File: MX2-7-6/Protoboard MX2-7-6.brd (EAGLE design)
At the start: 54.2 x 59.2 mm, 294 parts

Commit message: Update Gerb files
Created Gerber files for MX 2-7-6 without ESP
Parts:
- added U2: (no value), SparkFun-PowerIC:SOT23-5
- moved PAD442 1.27 mm to (27.9, 7.62)
- moved PAD443 1.27 mm to (40.6, 7.62)
- moved PAD444 1.27 mm to (5.08, 7.62)
- moved PAD445 1.27 mm to (43.2, 7.62)
- moved PAD446 1.27 mm to (38.1, 7.62)
- moved PAD447 1.27 mm to (7.62, 7.62)
- moved PAD448 1.27 mm to (50.8, 7.62)
- moved PAD449 1.27 mm to (35.6, 7.62)
- moved PAD450 1.27 mm to (10.2, 7.62)
- moved PAD451 1.27 mm to (48.3, 7.62)
- moved PAD452 1.27 mm to (33.0, 7.62)
- moved PAD453 1.27 mm to (12.7, 7.62)
- moved PAD454 1.27 mm to (45.7, 7.62)
- moved PAD455 1.27 mm to (30.5, 7.62)
- moved PAD456 1.27 mm to (15.2, 7.62)
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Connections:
- net GND: now also U2.2
- net VCC: now also U2.1, U2.3
- net VDD: now also U2.5
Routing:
- net VCC: track 12.5 -> 23.9 mm
- net VDD: track 133.6 -> 138.2 mm

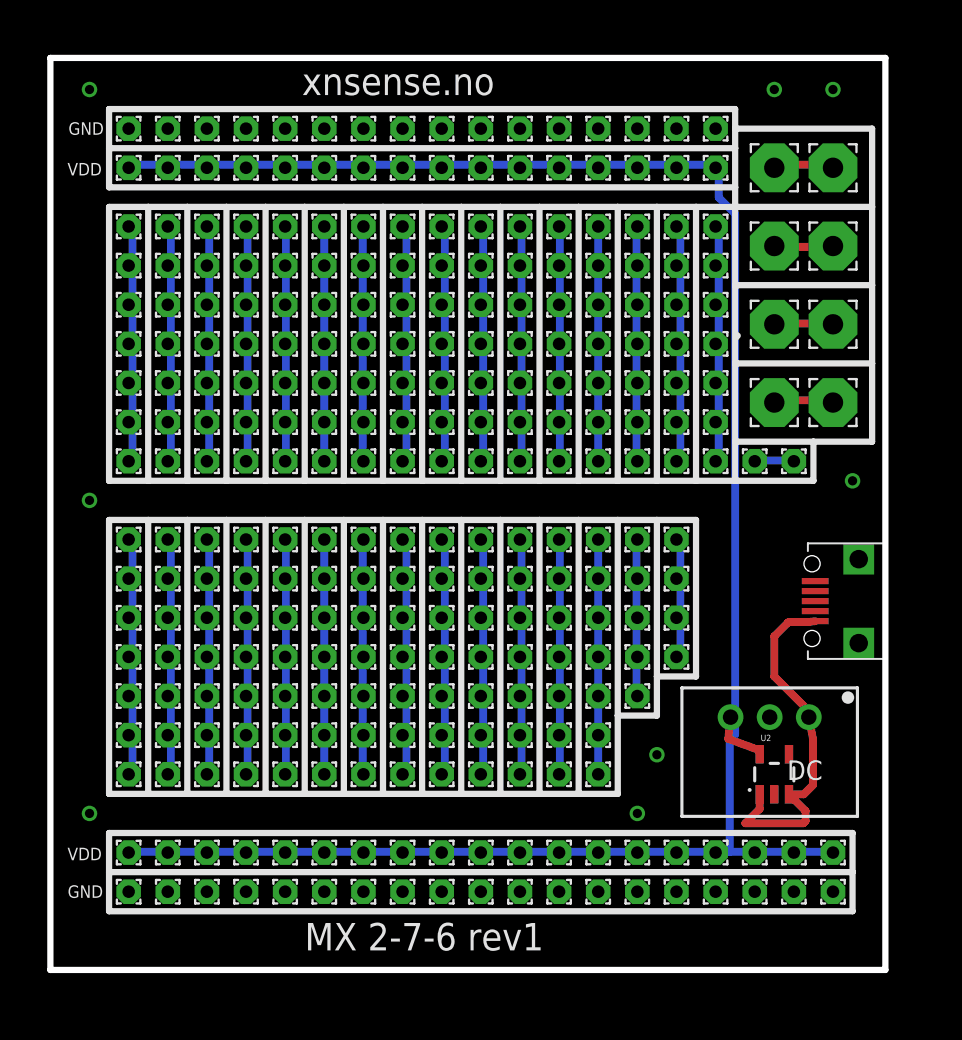
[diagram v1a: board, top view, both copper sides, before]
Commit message: Update to rev2
Updated to Pin headers instead of single wire pads
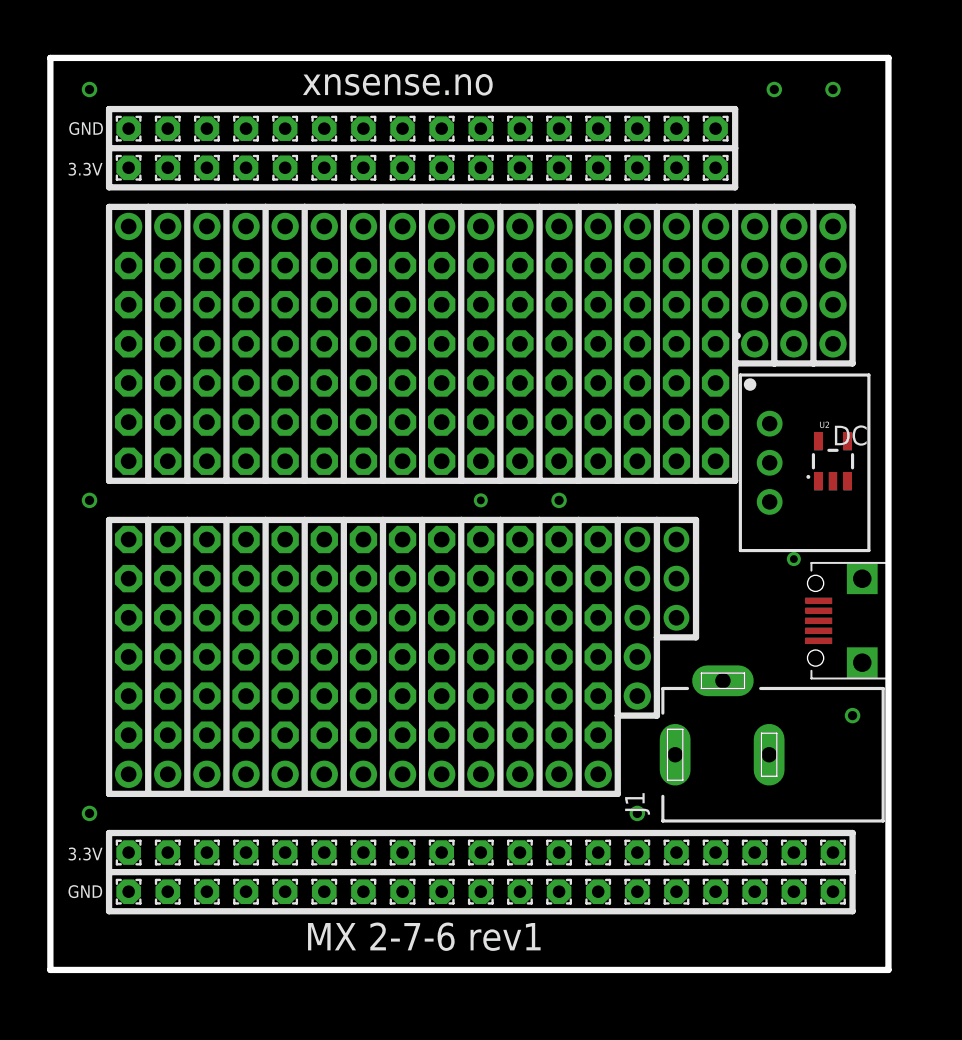
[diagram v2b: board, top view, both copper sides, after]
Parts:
- removed PAD1, PAD100, PAD101, PAD102, PAD103, PAD106, PAD107, PAD108, PAD109, PAD110, PAD111, PAD112, PAD115, PAD116, PAD117, PAD118, PAD119, PAD120, PAD121, PAD124, PAD125, PAD126, PAD127, PAD128, PAD129, PAD130, PAD133, PAD134, PAD135, PAD136, PAD137, PAD138, PAD139, PAD142, PAD143, PAD144, PAD145, PAD146, PAD147, PAD148, PAD151, PAD152, PAD153, PAD154, PAD155, PAD156, PAD157, PAD160, PAD161, PAD162, PAD163, PAD164, PAD165, PAD166, PAD169, PAD170, PAD171, PAD172, PAD173, PAD174, PAD175, PAD178, PAD179, PAD180, PAD181, PAD182, PAD183, PAD184, PAD187, PAD188, PAD189, PAD190, PAD191, PAD192, PAD193, PAD196, PAD197, PAD198, PAD199, PAD2, PAD200, PAD201, PAD202, PAD205, PAD206, PAD207, PAD208, PAD209, PAD210, PAD211, PAD214, PAD215, PAD216, PAD217, PAD218, PAD219, PAD220, PAD260, PAD261, PAD262, PAD263, PAD264, PAD265, PAD266, PAD269, PAD270, PAD271, PAD272, PAD273, PAD274, PAD275, PAD278, PAD279, PAD280, PAD281, PAD282, PAD283, PAD284, PAD287, PAD288, PAD289, PAD290, PAD291, PAD292, PAD293, PAD296, PAD297, PAD298, PAD299, PAD300, PAD301, PAD302, PAD305, PAD306, PAD307, PAD308, PAD309, PAD310, PAD311, PAD314, PAD315, PAD316, PAD317, PAD318, PAD319, PAD320, PAD332, PAD333, PAD334, PAD335, PAD336, PAD337, PAD338, PAD341, PAD342, PAD343, PAD344, PAD345, PAD346, PAD347, PAD350, PAD351, PAD352, PAD353, PAD354, PAD355, PAD356, PAD359, PAD360, PAD361, PAD362, PAD363, PAD364, PAD365, PAD368, PAD369, PAD370, PAD371, PAD372, PAD373, PAD374, PAD377, PAD378, PAD379, PAD380, PAD381, PAD382, PAD383, PAD385, PAD386, PAD387, PAD388, PAD389, PAD391, PAD392, PAD393, PAD394, PAD79, PAD80, PAD81, PAD82, PAD83, PAD84, PAD85, PAD88, PAD89, PAD90, PAD91, PAD92, PAD93, PAD94, PAD97, PAD98, PAD99: (no value), wirepad:1,6/0,8
- removed PAD34, PAD35, PAD39, PAD40, PAD42, PAD43, PAD45, PAD46: (no value), wirepad:3,17/1,3
- added CN1, CN2, CN3: 1X4-CLEANBIG, adafruit:1X04-CLEANBIG
- added J1: DCJ0202, con-jack:DCJ0202
- added JP10, JP11, JP12, JP13, JP14, JP15, JP16, JP17, JP18, JP19, JP2, JP20, JP21, JP22, JP23, JP24, JP25, JP26, JP27, JP28, JP29, JP3, JP30, JP4, JP5, JP6, JP7, JP8, JP9: (no value), adafruit:1X06-CLEANBIG
- added JP31, JP32: (no value), adafruit:1X03-CLEANBIG
- added JP33, JP34, JP35, JP36, JP37, JP38, JP39, JP40, JP41, JP42, JP43, JP44, JP45, JP46, JP47, JP48, JP49, JP50, JP51, JP52, JP53, JP54, JP55, JP56, JP57, JP58, JP59, JP60, JP61, JP62, JP63: (no value), adafruit:1X01-CLEANBIG
- moved U2 20.7 mm to (50.8, 33.0)
- moved DC 16.5 mm to (46.7, 32.9), turned to 270 degrees
- moved JP1 1.29 mm to (54.4, 22.7)
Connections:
- removed net N$40: PAD377.1, PAD378.1, PAD379.1, PAD380.1, PAD381.1, PAD382.1, PAD383.1
- removed net N$41: PAD385.1, PAD386.1, PAD387.1, PAD388.1, PAD389.1
- net GND: now also J1.2, J1.3
- net N$1: now also JP2.1, JP2.2, JP2.3, JP2.4, JP2.5, JP2.6, JP48.1; no longer PAD391.1, PAD392.1, PAD393.1, PAD394.1
- net N$10: now also JP54.1, JP9.1, JP9.2, JP9.3, JP9.4, JP9.5, JP9.6; no longer PAD106.1, PAD107.1, PAD108.1, PAD109.1, PAD110.1, PAD111.1, PAD112.1
- net N$11: now also JP10.1, JP10.2, JP10.3, JP10.4, JP10.5, JP10.6, JP55.1; no longer PAD115.1, PAD116.1, PAD117.1, PAD118.1, PAD119.1, PAD120.1, PAD121.1
- net N$12: now also JP11.1, JP11.2, JP11.3, JP11.4, JP11.5, JP11.6, JP56.1; no longer PAD124.1, PAD125.1, PAD126.1, PAD127.1, PAD128.1, PAD129.1, PAD130.1
- net N$13: now also JP12.1, JP12.2, JP12.3, JP12.4, JP12.5, JP12.6, JP57.1; no longer PAD133.1, PAD134.1, PAD135.1, PAD136.1, PAD137.1, PAD138.1, PAD139.1
- net N$14: now also JP13.1, JP13.2, JP13.3, JP13.4, JP13.5, JP13.6, JP58.1; no longer PAD142.1, PAD143.1, PAD144.1, PAD145.1, PAD146.1, PAD147.1, PAD148.1
- net N$15: now also JP14.1, JP14.2, JP14.3, JP14.4, JP14.5, JP14.6, JP59.1; no longer PAD151.1, PAD152.1, PAD153.1, PAD154.1, PAD155.1, PAD156.1, PAD157.1
- net N$16: now also JP15.1, JP15.2, JP15.3, JP15.4, JP15.5, JP15.6, JP60.1; no longer PAD160.1, PAD161.1, PAD162.1, PAD163.1, PAD164.1, PAD165.1, PAD166.1
- net N$17: now also JP16.1, JP16.2, JP16.3, JP16.4, JP16.5, JP16.6, JP61.1; no longer PAD169.1, PAD170.1, PAD171.1, PAD172.1, PAD173.1, PAD174.1, PAD175.1
- net N$18: now also JP4.1, JP4.2, JP4.3, JP4.4, JP4.5, JP4.6, JP62.1; no longer PAD178.1, PAD179.1, PAD180.1, PAD181.1, PAD182.1, PAD183.1, PAD184.1
- net N$19: now also JP17.1, JP17.2, JP17.3, JP17.4, JP17.5, JP17.6, JP63.1; no longer PAD187.1, PAD188.1, PAD189.1, PAD190.1, PAD191.1, PAD192.1, PAD193.1
- net N$2: now also CN1.1, CN1.2, CN1.3, CN1.4; no longer PAD34.1, PAD35.1
- net N$20: now also JP18.1, JP18.2, JP18.3, JP18.4, JP18.5, JP18.6, JP34.1; no longer PAD196.1, PAD197.1, PAD198.1, PAD199.1, PAD200.1, PAD201.1, PAD202.1
- net N$21: now also JP19.1, JP19.2, JP19.3, JP19.4, JP19.5, JP19.6, JP35.1; no longer PAD205.1, PAD206.1, PAD207.1, PAD208.1, PAD209.1, PAD210.1, PAD211.1
- net N$22: now also JP20.1, JP20.2, JP20.3, JP20.4, JP20.5, JP20.6, JP36.1; no longer PAD214.1, PAD215.1, PAD216.1, PAD217.1, PAD218.1, PAD219.1, PAD220.1
- net N$27: now also JP21.1, JP21.2, JP21.3, JP21.4, JP21.5, JP21.6, JP37.1; no longer PAD260.1, PAD261.1, PAD262.1, PAD263.1, PAD264.1, PAD265.1, PAD266.1
- net N$28: now also JP22.1, JP22.2, JP22.3, JP22.4, JP22.5, JP22.6, JP38.1; no longer PAD269.1, PAD270.1, PAD271.1, PAD272.1, PAD273.1, PAD274.1, PAD275.1
- net N$29: now also JP23.1, JP23.2, JP23.3, JP23.4, JP23.5, JP23.6, JP39.1; no longer PAD278.1, PAD279.1, PAD280.1, PAD281.1, PAD282.1, PAD283.1, PAD284.1
- net N$3: now also CN2.1, CN2.2, CN2.3, CN2.4; no longer PAD1.1, PAD2.1
- net N$30: now also JP24.1, JP24.2, JP24.3, JP24.4, JP24.5, JP24.6, JP40.1; no longer PAD287.1, PAD288.1, PAD289.1, PAD290.1, PAD291.1, PAD292.1, PAD293.1
- net N$31: now also JP25.1, JP25.2, JP25.3, JP25.4, JP25.5, JP25.6, JP41.1; no longer PAD296.1, PAD297.1, PAD298.1, PAD299.1, PAD300.1, PAD301.1, PAD302.1
- net N$32: now also JP26.1, JP26.2, JP26.3, JP26.4, JP26.5, JP26.6, JP42.1; no longer PAD305.1, PAD306.1, PAD307.1, PAD308.1, PAD309.1, PAD310.1, PAD311.1
- net N$33: now also JP27.1, JP27.2, JP27.3, JP27.4, JP27.5, JP27.6, JP43.1; no longer PAD314.1, PAD315.1, PAD316.1, PAD317.1, PAD318.1, PAD319.1, PAD320.1
- net N$35: now also JP28.1, JP28.2, JP28.3, JP28.4, JP28.5, JP28.6, JP44.1; no longer PAD332.1, PAD333.1, PAD334.1, PAD335.1, PAD336.1, PAD337.1, PAD338.1
- net N$36: now also JP29.1, JP29.2, JP29.3, JP29.4, JP29.5, JP29.6, JP45.1; no longer PAD341.1, PAD342.1, PAD343.1, PAD344.1, PAD345.1, PAD346.1, PAD347.1
- net N$37: now also JP30.1, JP30.2, JP30.3, JP30.4, JP30.5, JP30.6, JP46.1; no longer PAD350.1, PAD351.1, PAD352.1, PAD353.1, PAD354.1, PAD355.1, PAD356.1
- net N$38: now also JP31.1, JP31.2, JP31.3, JP33.1, JP47.1; no longer PAD359.1, PAD360.1, PAD361.1, PAD362.1, PAD363.1, PAD364.1, PAD365.1
- net N$39: now also JP32.1, JP32.2, JP32.3; no longer PAD368.1, PAD369.1, PAD370.1, PAD371.1, PAD372.1, PAD373.1, PAD374.1
- net N$4: now also CN3.1, CN3.2, CN3.3, CN3.4; no longer PAD39.1, PAD40.1
- net N$5: now also JP3.1, JP3.2, JP3.3, JP3.4, JP3.5, JP3.6, JP49.1; no longer PAD42.1, PAD43.1
- net N$6: now also JP5.1, JP5.2, JP5.3, JP5.4, JP5.5, JP5.6, JP50.1; no longer PAD45.1, PAD46.1
- net N$7: now also JP51.1, JP6.1, JP6.2, JP6.3, JP6.4, JP6.5, JP6.6; no longer PAD79.1, PAD80.1, PAD81.1, PAD82.1, PAD83.1, PAD84.1, PAD85.1
- net N$8: now also JP52.1, JP7.1, JP7.2, JP7.3, JP7.4, JP7.5, JP7.6; no longer PAD88.1, PAD89.1, PAD90.1, PAD91.1, PAD92.1, PAD93.1, PAD94.1
- net N$9: now also JP53.1, JP8.1, JP8.2, JP8.3, JP8.4, JP8.5, JP8.6; no longer PAD100.1, PAD101.1, PAD102.1, PAD103.1, PAD97.1, PAD98.1, PAD99.1
- net VCC: now also J1.1
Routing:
- net VDD: track 138.2 -> 0.00 mm
- net VCC: track 23.9 -> 0.00 mm
- net N$40: track 16.9 -> 0.00 mm, vias 0 -> 1
- net N$27: track 16.9 -> 0.00 mm
- net N$17: track 16.9 -> 0.00 mm
- net N$9: track 16.9 -> 0.00 mm
- net N$22: track 16.9 -> 0.00 mm
- net N$35: track 16.5 -> 0.00 mm
- net N$28: track 16.5 -> 0.00 mm
- net N$21: track 16.5 -> 0.00 mm
- net N$12: track 16.5 -> 0.00 mm
- net N$10: track 16.5 -> 0.00 mm
- net N$36: track 16.1 -> 0.00 mm
- net N$29: track 16.1 -> 0.00 mm
- net N$7: track 16.0 -> 0.00 mm
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- added copper zone on layer 16, net N$45
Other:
- board size 54.2 x 59.2 mm -> 54.4 x 59.2 mm
- board text added: "3.3V"
- board text removed: "VDD"

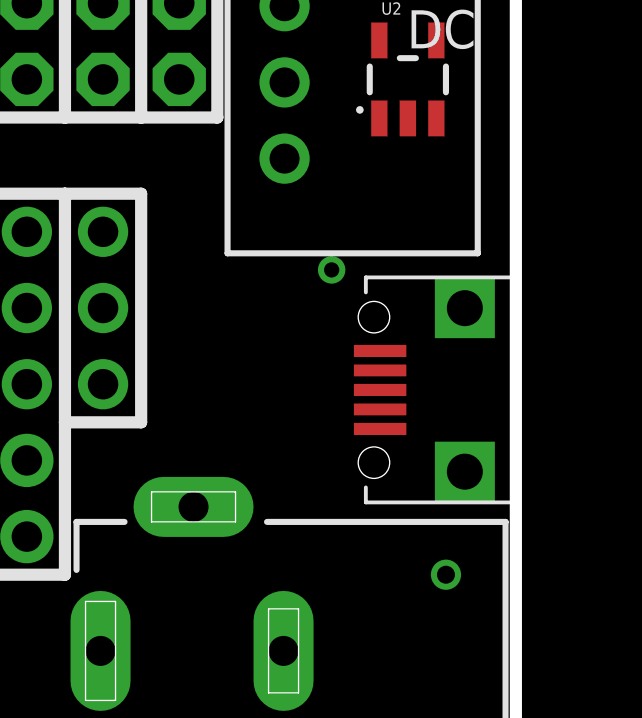
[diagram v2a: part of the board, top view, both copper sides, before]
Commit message: Change usb connector
Change to correct usb connecter and moved esp8266 bit more onto the
board.
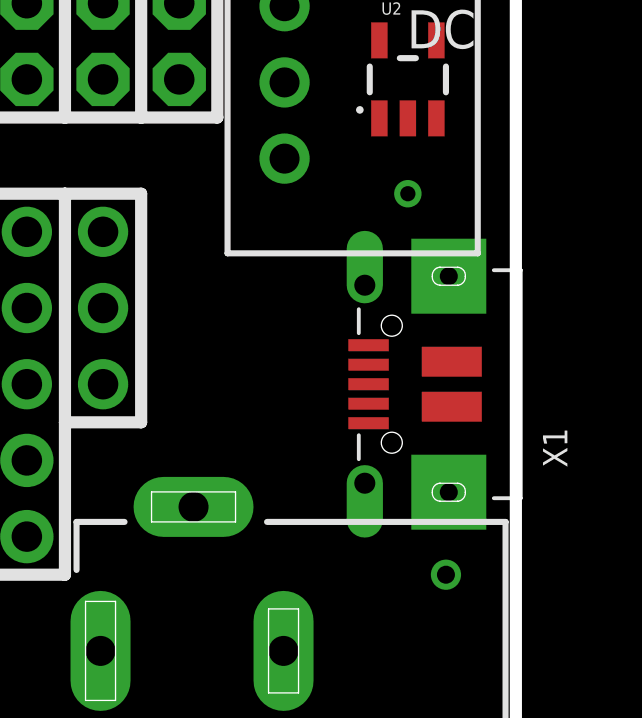
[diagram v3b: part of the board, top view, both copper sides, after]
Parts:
- removed JP1: USB-RECEPTABLE, daspilker:FCI-10103594-0001LF
- added X1: (no value), microbuilder:4UCONN_20329
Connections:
- net GND: now also X1.BASE@1, X1.BASE@2, X1.GND, X1.SPRT@1, X1.SPRT@2, X1.SPRT@3, X1.SPRT@4; no longer JP1.5
- net VCC: now also X1.VBUS; no longer JP1.1

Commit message: Update esp component and usb
test
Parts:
- removed JP10, JP11, JP12, JP13, JP14, JP15, JP16, JP17, JP18, JP19, JP2, JP20, JP21, JP22, JP23, JP24, JP25, JP26, JP27, JP28, JP29, JP3, JP30, JP4, JP5, JP6, JP7, JP8, JP9: (no value), adafruit:1X06-CLEANBIG
- removed JP31, JP32: (no value), adafruit:1X03-CLEANBIG
- removed JP33, JP34, JP35, JP36, JP37, JP38, JP39, JP40, JP41, JP42, JP43, JP44, JP45, JP46, JP47, JP48, JP49, JP50, JP51, JP52, JP53, JP54, JP55, JP56, JP57, JP58, JP59, JP60, JP61, JP62, JP63: (no value), adafruit:1X01-CLEANBIG
- added J10, J11, J12, J13, J14, J15, J16, J17, J18, J19, J2, J20, J21, J22, J23, J24, J25, J26, J27, J28, J29, J3, J30, J4, J5, J6, J7, J8, J9: (no value), SparkFun-Connectors:1X07_NO_SILK
- added J31: (no value), SparkFun-Connectors:1X05_NO_SILK
- added J32: (no value), SparkFun-Connectors:1X03_NO_SILK
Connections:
- net N$1: now also J2.1, J2.2, J2.3, J2.4, J2.5, J2.6, J2.7; no longer JP2.1, JP2.2, JP2.3, JP2.4, JP2.5, JP2.6, JP48.1
- net N$10: now also J8.1, J8.2, J8.3, J8.4, J8.5, J8.6, J8.7; no longer JP54.1, JP9.1, JP9.2, JP9.3, JP9.4, JP9.5, JP9.6
- net N$11: now also J9.1, J9.2, J9.3, J9.4, J9.5, J9.6, J9.7; no longer JP10.1, JP10.2, JP10.3, JP10.4, JP10.5, JP10.6, JP55.1
- net N$12: now also J10.1, J10.2, J10.3, J10.4, J10.5, J10.6, J10.7; no longer JP11.1, JP11.2, JP11.3, JP11.4, JP11.5, JP11.6, JP56.1
- net N$13: now also J11.1, J11.2, J11.3, J11.4, J11.5, J11.6, J11.7; no longer JP12.1, JP12.2, JP12.3, JP12.4, JP12.5, JP12.6, JP57.1
- net N$14: now also J12.1, J12.2, J12.3, J12.4, J12.5, J12.6, J12.7; no longer JP13.1, JP13.2, JP13.3, JP13.4, JP13.5, JP13.6, JP58.1
- net N$15: now also J13.1, J13.2, J13.3, J13.4, J13.5, J13.6, J13.7; no longer JP14.1, JP14.2, JP14.3, JP14.4, JP14.5, JP14.6, JP59.1
- net N$16: now also J14.1, J14.2, J14.3, J14.4, J14.5, J14.6, J14.7; no longer JP15.1, JP15.2, JP15.3, JP15.4, JP15.5, JP15.6, JP60.1
- net N$17: now also J15.1, J15.2, J15.3, J15.4, J15.5, J15.6, J15.7; no longer JP16.1, JP16.2, JP16.3, JP16.4, JP16.5, JP16.6, JP61.1
- net N$18: now also J16.1, J16.2, J16.3, J16.4, J16.5, J16.6, J16.7; no longer JP4.1, JP4.2, JP4.3, JP4.4, JP4.5, JP4.6, JP62.1
- net N$19: now also J17.1, J17.2, J17.3, J17.4, J17.5, J17.6, J17.7; no longer JP17.1, JP17.2, JP17.3, JP17.4, JP17.5, JP17.6, JP63.1
- net N$20: now also J18.1, J18.2, J18.3, J18.4, J18.5, J18.6, J18.7; no longer JP18.1, JP18.2, JP18.3, JP18.4, JP18.5, JP18.6, JP34.1
- net N$21: now also J19.1, J19.2, J19.3, J19.4, J19.5, J19.6, J19.7; no longer JP19.1, JP19.2, JP19.3, JP19.4, JP19.5, JP19.6, JP35.1
- net N$22: now also J20.1, J20.2, J20.3, J20.4, J20.5, J20.6, J20.7; no longer JP20.1, JP20.2, JP20.3, JP20.4, JP20.5, JP20.6, JP36.1
- net N$27: now also J21.1, J21.2, J21.3, J21.4, J21.5, J21.6, J21.7; no longer JP21.1, JP21.2, JP21.3, JP21.4, JP21.5, JP21.6, JP37.1
- net N$28: now also J22.1, J22.2, J22.3, J22.4, J22.5, J22.6, J22.7; no longer JP22.1, JP22.2, JP22.3, JP22.4, JP22.5, JP22.6, JP38.1
- net N$29: now also J23.1, J23.2, J23.3, J23.4, J23.5, J23.6, J23.7; no longer JP23.1, JP23.2, JP23.3, JP23.4, JP23.5, JP23.6, JP39.1
- net N$30: now also J24.1, J24.2, J24.3, J24.4, J24.5, J24.6, J24.7; no longer JP24.1, JP24.2, JP24.3, JP24.4, JP24.5, JP24.6, JP40.1
- net N$31: now also J25.1, J25.2, J25.3, J25.4, J25.5, J25.6, J25.7; no longer JP25.1, JP25.2, JP25.3, JP25.4, JP25.5, JP25.6, JP41.1
- net N$32: now also J26.1, J26.2, J26.3, J26.4, J26.5, J26.6, J26.7; no longer JP26.1, JP26.2, JP26.3, JP26.4, JP26.5, JP26.6, JP42.1
- net N$33: now also J27.1, J27.2, J27.3, J27.4, J27.5, J27.6, J27.7; no longer JP27.1, JP27.2, JP27.3, JP27.4, JP27.5, JP27.6, JP43.1
- net N$35: now also J28.1, J28.2, J28.3, J28.4, J28.5, J28.6, J28.7; no longer JP28.1, JP28.2, JP28.3, JP28.4, JP28.5, JP28.6, JP44.1
- net N$36: now also J29.1, J29.2, J29.3, J29.4, J29.5, J29.6, J29.7; no longer JP29.1, JP29.2, JP29.3, JP29.4, JP29.5, JP29.6, JP45.1
- net N$37: now also J30.1, J30.2, J30.3, J30.4, J30.5, J30.6, J30.7; no longer JP30.1, JP30.2, JP30.3, JP30.4, JP30.5, JP30.6, JP46.1
- net N$38: now also J31.1, J31.2, J31.3, J31.4, J31.5; no longer JP31.1, JP31.2, JP31.3, JP33.1, JP47.1
- net N$39: now also J32.1, J32.2, J32.3; no longer JP32.1, JP32.2, JP32.3
- net N$5: now also J3.1, J3.2, J3.3, J3.4, J3.5, J3.6, J3.7; no longer JP3.1, JP3.2, JP3.3, JP3.4, JP3.5, JP3.6, JP49.1
- net N$6: now also J4.1, J4.2, J4.3, J4.4, J4.5, J4.6, J4.7; no longer JP5.1, JP5.2, JP5.3, JP5.4, JP5.5, JP5.6, JP50.1
- net N$7: now also J5.1, J5.2, J5.3, J5.4, J5.5, J5.6, J5.7; no longer JP51.1, JP6.1, JP6.2, JP6.3, JP6.4, JP6.5, JP6.6
- net N$8: now also J6.1, J6.2, J6.3, J6.4, J6.5, J6.6, J6.7; no longer JP52.1, JP7.1, JP7.2, JP7.3, JP7.4, JP7.5, JP7.6
- net N$9: now also J7.1, J7.2, J7.3, J7.4, J7.5, J7.6, J7.7; no longer JP53.1, JP8.1, JP8.2, JP8.3, JP8.4, JP8.5, JP8.6

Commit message: Routed
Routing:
- net VDD: track 0.00 -> 149.6 mm, vias 0 -> 1
- net VCC: track 0.00 -> 35.0 mm, vias 0 -> 1
- net N$37: track 0.00 -> 15.2 mm
- net N$36: track 0.00 -> 15.2 mm
- net N$35: track 0.00 -> 15.2 mm
- net N$33: track 0.00 -> 15.2 mm
- net N$32: track 0.00 -> 15.2 mm
- net N$31: track 0.00 -> 15.2 mm
- net N$30: track 0.00 -> 15.2 mm
- net N$29: track 0.00 -> 15.2 mm
- net N$28: track 0.00 -> 15.2 mm
- net N$27: track 0.00 -> 15.2 mm
- net N$22: track 0.00 -> 15.2 mm
- net N$21: track 0.00 -> 15.2 mm
- net N$20: track 0.00 -> 15.2 mm
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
